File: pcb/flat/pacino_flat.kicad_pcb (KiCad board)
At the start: 2 copper layers, 139.1 x 114.2 mm, 47 parts, among them SW1 MX_Hotswap_Rev, SW10 MX_Hotswap_Rev, SW11 MX_Hotswap_Rev, SW12 MX_Hotswap_Rev, SW13 MX_Hotswap_Rev, SW14 MX_Hotswap_Rev, SW15 MX_Hotswap_Rev, SW16 MX_Hotswap_Rev, SW17 MX_Hotswap_Rev, SW18 MX_Hotswap_Rev, SW19 MX_Hotswap_Rev, SW2 MX_Hotswap_Rev, SW20 MX_Hotswap_Rev, SW3 MX_Hotswap_Rev, SW4 MX_Hotswap_Rev, SW5 MX_Hotswap_Rev, SW6 MX_Hotswap_Rev, SW7 MX_Hotswap_Rev, SW8 MX_Hotswap_Rev, SW9 MX_Hotswap_Rev, U1 nice!nano

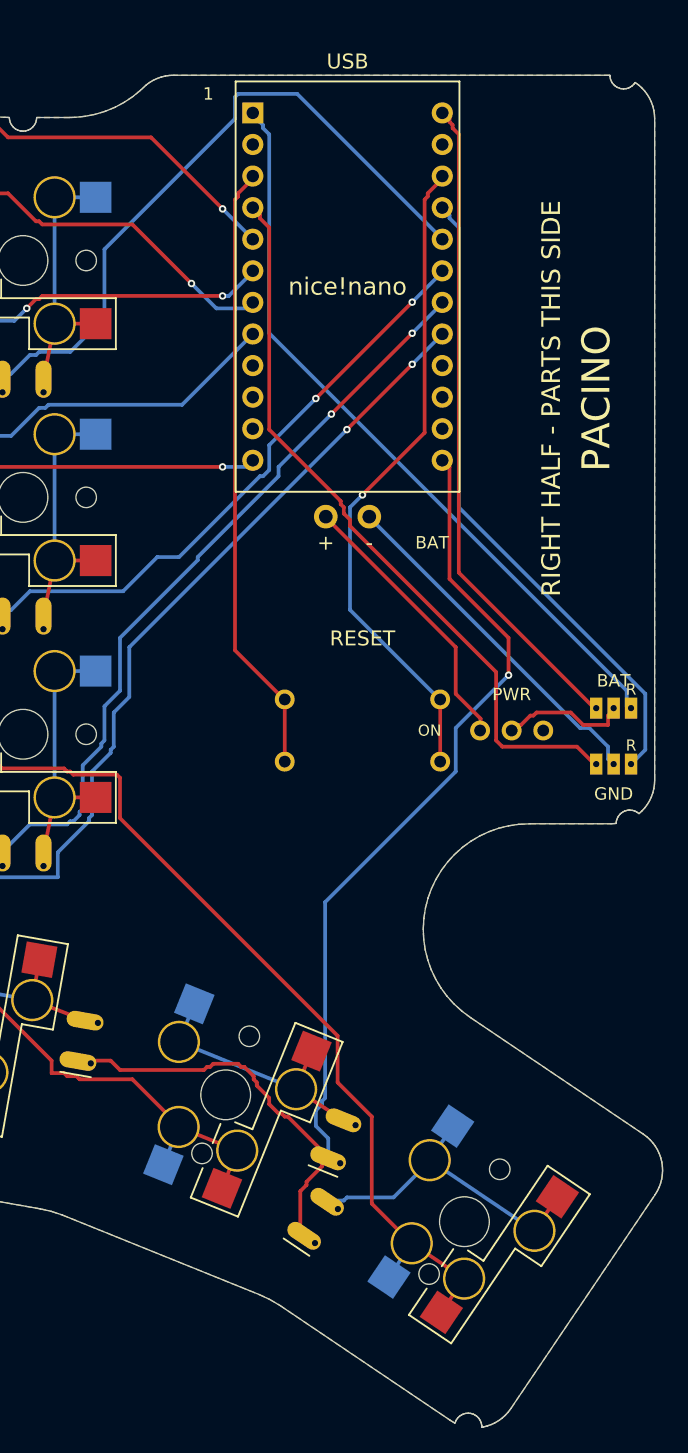
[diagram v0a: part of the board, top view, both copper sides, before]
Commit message: Slim build: screw channels up the wall over the insert holes, 3 mm wall, three pillars pulled in
The pillars stop at the board while the wall keeps rising 5 mm past them, so the seven insert
holes on the wall line were tucked 1.2 mm under it: a half-moon from above, no way in for an
insert, and the screws would have sat 0.5 mm into the wall. Now a 4 mm channel (pcb_screw_channel)
runs up the inside of the wall over each hole, the slim case's wall is 3 mm (pcb_wall) so 1.5 mm
is left behind it, and the three pillars with room (thumb end, the bay's bottom corner, the one by
the thumb keys already was) stand 2.5-3 mm clear of the wall as full round bosses. Both boards
regenerated (five edge notches, three real holes); hand-wired builds unchanged.

Co-Authored-By: Claude Fable 5 <noreply@anthropic.com>
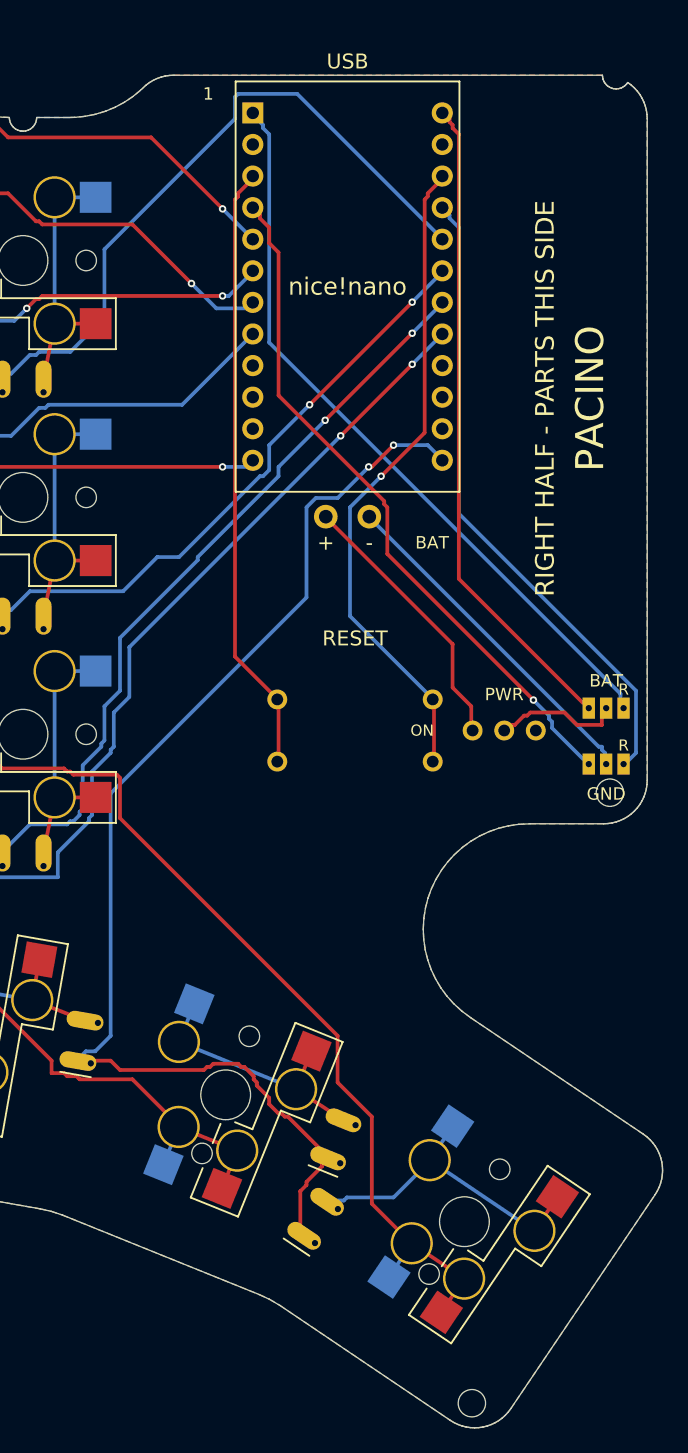
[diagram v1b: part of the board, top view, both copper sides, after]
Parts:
- added H2: MountingHole, pacino_flat:MountingHole, F.Cu at (172.3, 166.3)
- added H3: MountingHole, pacino_flat:MountingHole, F.Cu at (118.5, 124.4)
- moved H1 65.3 mm to (183.4, 117.2)
- moved JP1 0.60 mm to (183.1, 110.4)
- moved JP2 0.60 mm to (183.1, 114.9)
- moved PWR1 0.60 mm to (174.9, 112.2)
- moved RSW1 0.60 mm to (162.9, 112.2)
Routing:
- net GND_L: track 59.7 -> 55.9 mm, vias 0 -> 1
- net ROW4: track 96.8 -> 97.9 mm, vias 1 -> 2
- net GND: track 28.6 -> 28.0 mm
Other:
- board size 139.1 x 114.2 mm -> 139.1 x 114.3 mm

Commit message: PCB: controller on top of the board, reset legs paired the right way, jumpers clear of the boss
Three things the first batch of boards taught us:

- The nano sits on the face opposite the sockets (on top, flush in the plate window --
  what the case is built around), which swaps its pin rows relative to what the generator
  assumed. Per-half pin tables, the printed ZMK lists (right half columns inner-first) and
  the L/R silkscreen faces are now computed for that; MCU power nets renamed so the L pads
  serve the left half.
- A 12 mm tactile links its two legs 12.5 mm apart internally; the footprint had the 5 mm
  pairs on one net, so a normally fitted switch held RST at GND and the nano never booted.
- JP1/JP2 sat 2.3 mm from the bay's corner mounting hole, under its boss: a bridge there
  keeps the case from closing. Moved 4.5 mm up the strip, with a clearance guard.

Also: the nice!view goes on pro_micro 1/2/3 (ZMK's adapter), not 14/15/16 -- the hand-wired
build needs no rewiring; on the PCB a display needs its own SPI pins. Boards, gerbers,
renders and READMEs regenerated; overlays match the zmk-config copies.

Co-Authored-By: Claude Fable 5.1 <noreply@anthropic.com>
Claude-Session: https://claude.ai/code/session_01BAXTGjnxuhw6nNKSjTcvZb
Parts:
- moved JP1 4.50 mm to (183.1, 105.9)
- moved JP2 4.50 mm to (183.1, 110.4)
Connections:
- U1 pad 1: BAT_R -> BAT_L
- U1 pad 21: GND_R -> GND_L
- U1 pad 24: BAT_L -> BAT_R
- U1 pad 4: GND_L -> GND_R
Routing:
- net COL4: track 156.1 -> 167.2 mm, vias 1 -> 2
- net BAT_R: track 60.3 -> 49.5 mm
- net RST_B: track 53.2 -> 62.8 mm, vias 1 -> 2
- net RST_A: track 49.3 -> 56.8 mm
- net GND_L: track 55.9 -> 49.1 mm
- net GND_R: track 51.6 -> 58.3 mm
- net COL2: track 205.4 -> 210.6 mm
- net ROW4: track 97.9 -> 94.6 mm
- net COL0: track 174.0 -> 176.0 mm, vias 1 -> 0
- net COL1: track 172.8 -> 174.9 mm, vias 3 -> 1
- net GND: track 28.0 -> 26.2 mm
- net BAT_L: track 52.9 -> 54.7 mm
- net ROW0: track 141.0 -> 139.6 mm
- net BAT_SW: track 10.1 -> 11.2 mm
- net COL3: track 169.4 -> 170.4 mm, vias 2 -> 3
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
